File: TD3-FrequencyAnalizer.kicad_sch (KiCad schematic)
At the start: 0 parts

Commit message: Update project files and add schematic sheets (ESP32-S3, Alimentacion, Acondicionamiento, Salida)
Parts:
- added C1: C, symbol Device:C
- added D1: BAT54S, Package_TO_SOT_SMD:SOT-23, symbol Diode:BAT54S
- added R1: R, symbol Device:R
- added RV1: R_Potentiometer, symbol Device:R_Potentiometer
- added TP1: TestPoint, symbol Connector:TestPoint
- added U3: TL072, symbol Amplifier_Operational:TL072
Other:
- added sheet Acondicionamiento de Señal de Entrada (Acondicionamiento_de_señal.kicad_sch)
- added sheet Alimentación (Alimentación.kicad_sch)
- added sheet ESP32-S3 (ESP32-S3.kicad_sch)
- added sheet Señal de Salida (Señal de salida.kicad_sch)
- company: (none) -> UTN-Fra
- title: (none) -> Analizador de Respuesta en Frecuencia

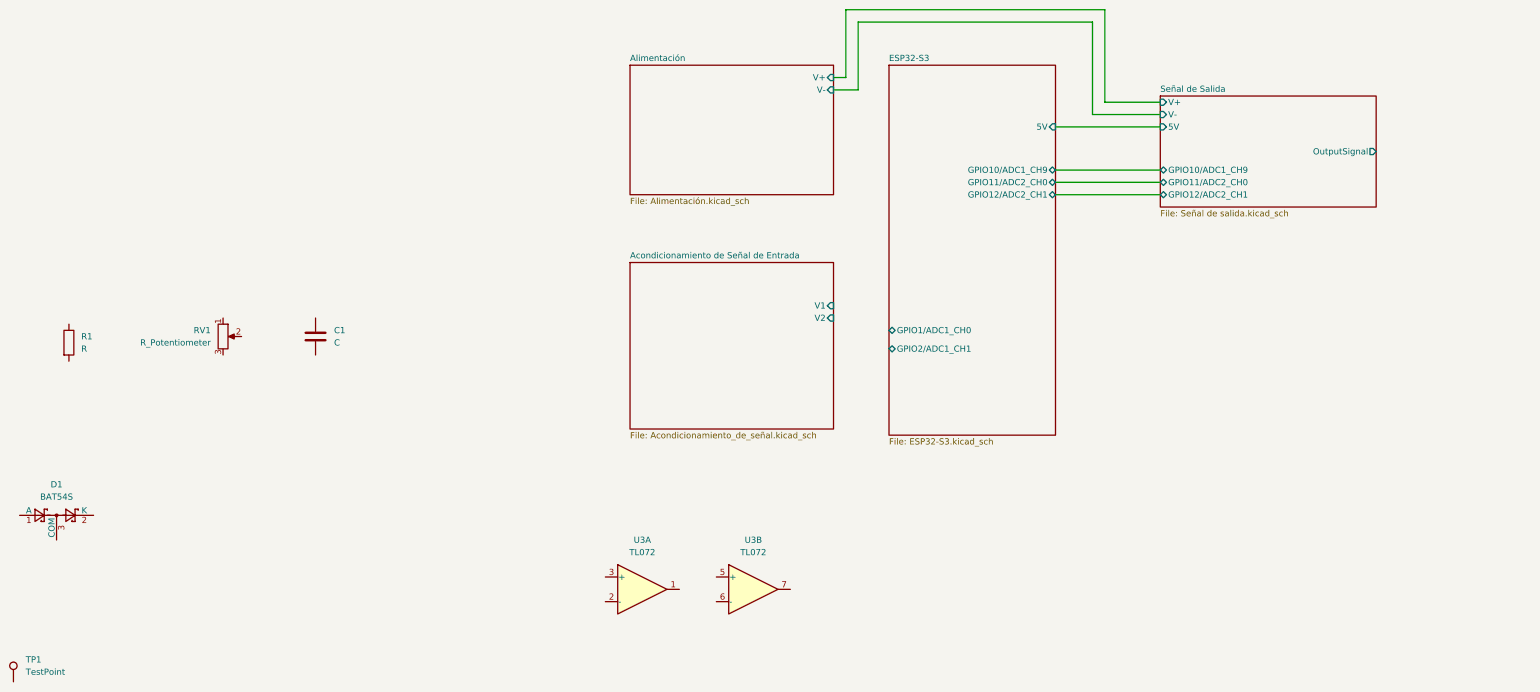
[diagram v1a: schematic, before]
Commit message: Update schematics: signal conditioning, power, ESP32-S3, output, and add signal measurement sub-sheet
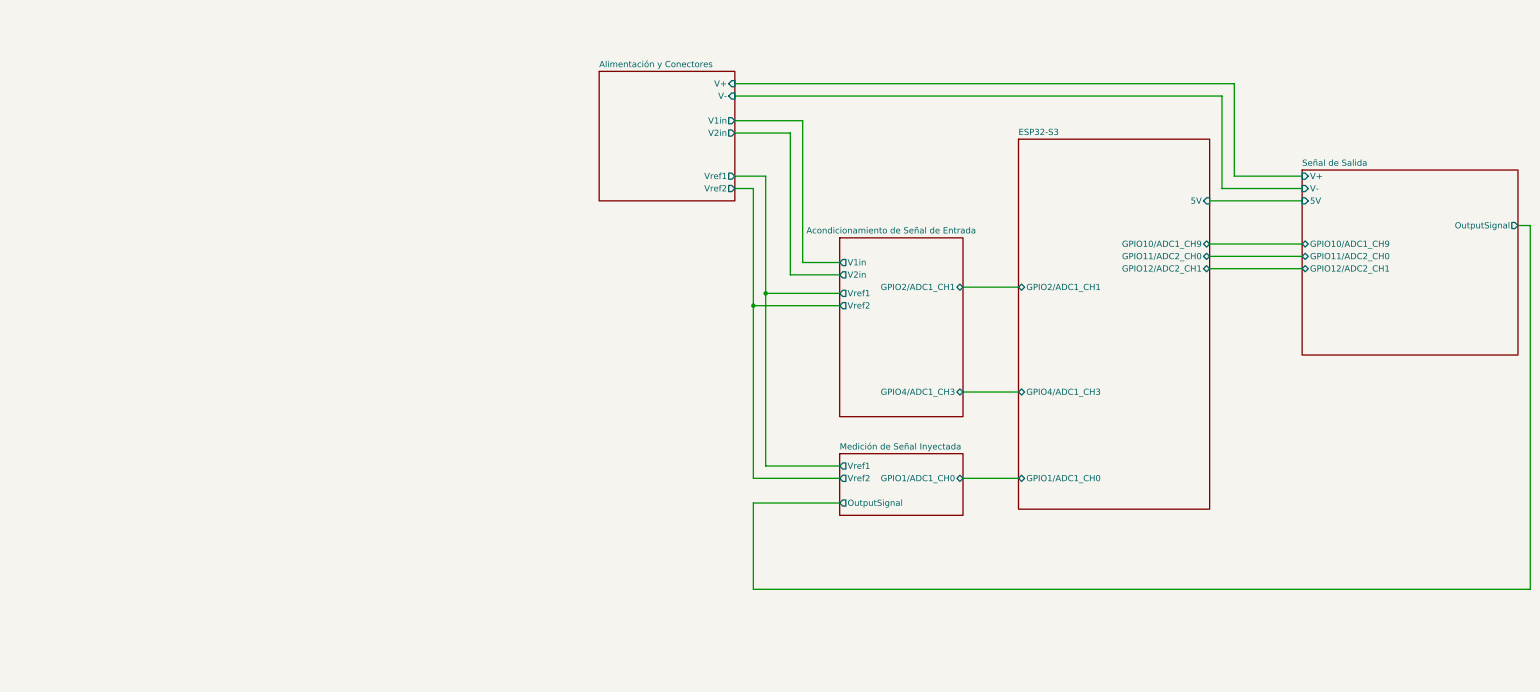
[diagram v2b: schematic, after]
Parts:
- removed C1: C, symbol Device:C
- removed D1: BAT54S, Package_TO_SOT_SMD:SOT-23, symbol Diode:BAT54S
- removed R1: R, symbol Device:R
- removed RV1: R_Potentiometer, symbol Device:R_Potentiometer
- removed TP1: TestPoint, symbol Connector:TestPoint
- removed U3: TL072, symbol Amplifier_Operational:TL072
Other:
- sheet Alimentación renamed Alimentación y Conectores
- added sheet Medición de Señal Inyectada (Medición de Señal Inyectada.kicad_sch)
- sheet Acondicionamiento de Señal de Entrada ports: added GPIO2/ADC1_CH1, GPIO4/ADC1_CH3, V1in, V2in, Vref1, Vref2; removed V1, V2
- sheet Alimentación y Conectores ports: added V1in, V2in, Vref1, Vref2; removed none
- sheet ESP32-S3 ports: added GPIO4/ADC1_CH3; removed none

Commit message: Save local schematic and board updates before 3D model path resolution
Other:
- sheet ESP32-S3 ports: added GPIO5/ADC1_CH4, GPIO6/ADC1_CH5, GPIO7/ADC1_CH6; removed none
- sheet Señal de Salida ports: added GPIO5/ADC1_CH4, GPIO6/ADC1_CH5, GPIO7/ADC1_CH6; removed none
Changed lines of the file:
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@@
+	(wire
+		(pts
+			(xy 170.18 83.82) (xy 189.23 83.82)
+		)
+		(stroke
+			(width 0)
+			(type default)
+		)
+	)
 	(wire
 		(pts
@@
 	(wire
 		(pts
+			(xy 170.18 87.63) (xy 189.23 87.63)
+		)
+		(stroke
+			(width 0)
+			(type default)
+		)
+	)
+	(wire
+		(pts
 			(xy 93.98 74.93) (xy 86.36 74.93)
 		)
@@
 		(pts
 			(xy 236.22 67.31) (xy 236.22 142.24)
+		)
+		(stroke
+			(width 0)
+			(type default)
+		)
+	)
+	(wire
+		(pts
+			(xy 170.18 91.44) (xy 189.23 91.44)
 		)
 		(stroke
@@
 			)
 		)
+		(pin "GPIO5/ADC1_CH4" bidirectional
+			(at 189.23 83.82 180)
+			(effects
+				(font
+					(size 1.27 1.27)
+				)
+				(justify left)
+			)
+		)
+		(pin "GPIO6/ADC1_CH5" bidirectional
+			(at 189.23 87.63 180)
+			(effects
+				(font
+					(size 1.27 1.27)
+				)
+				(justify left)
+			)
+		)
+		(pin "GPIO7/ADC1_CH6" bidirectional
+			(at 189.23 91.44 180)
+			(effects
+				(font
+					(size 1.27 1.27)
+				)
+				(justify left)
+			)
+		)
 		(instances
 			(project "TD3-FrequencyAnalizer"
@@
 			)
 		)
+		(pin "GPIO5/ADC1_CH4" bidirectional
+			(at 170.18 83.82 0)
+			(effects
+				(font
+					(size 1.27 1.27)
+				)
+				(justify right)
+			)
+		)
+		(pin "GPIO6/ADC1_CH5" bidirectional
+			(at 170.18 87.63 0)
+			(effects
+				(font
+					(size 1.27 1.27)
+				)
+				(justify right)
+			)
+		)
+		(pin "GPIO7/ADC1_CH6" bidirectional
+			(at 170.18 91.44 0)
+			(effects
+				(font
+					(size 1.27 1.27)
+				)
+				(justify right)
+			)
+		)
